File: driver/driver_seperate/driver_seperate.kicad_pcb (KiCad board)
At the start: 4 copper layers, 37.8 x 34.2 mm, 21 parts, among them IC1 MCT8316Z0TQRGFRQ1, J2 Motor, J3 Conn_01x05, J4 Conn_01x02

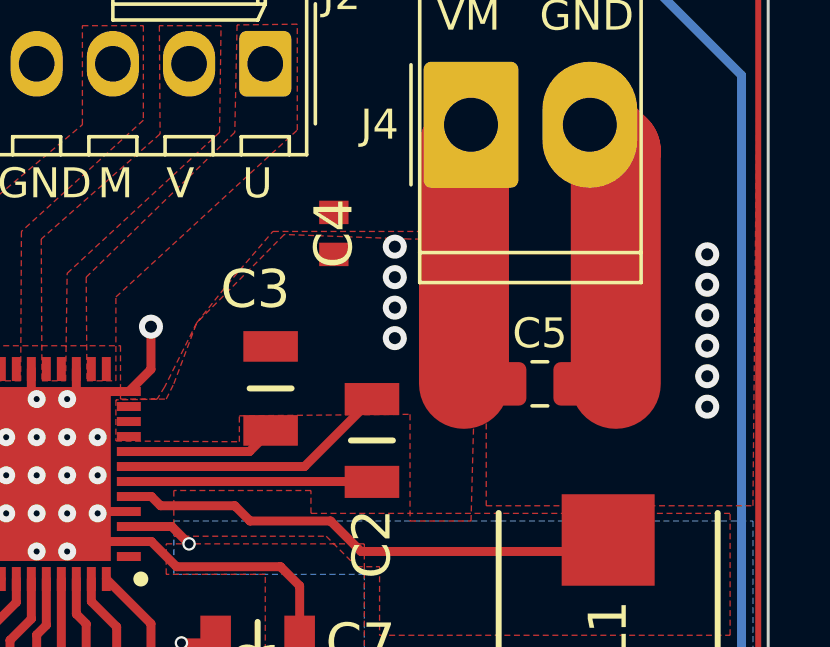
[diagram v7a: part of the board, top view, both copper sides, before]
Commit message: Move capacitor, change footprint to more common part
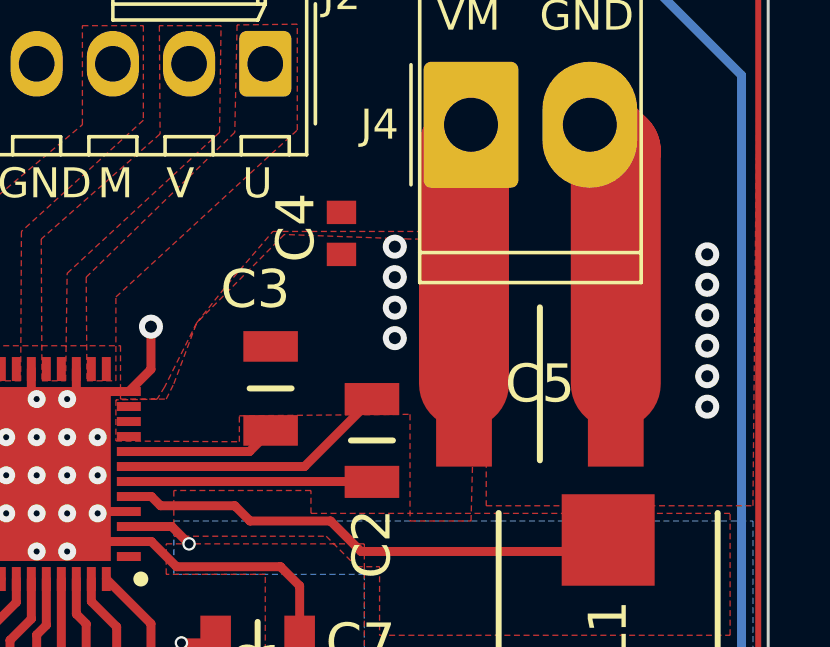
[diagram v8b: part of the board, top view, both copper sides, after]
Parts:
- C5: footprint Capacitor_SMD:C_0805_2012Metric -> SamacSys_Parts:CAPC6153X500N
- moved C4 0.25 mm to (132.6, 74.0)
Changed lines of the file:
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@@
   )
   (footprint "SamacSys_Parts:CAPC1608X95N" (layer "F.Cu")
-    (at 132.334 73.98 90)
+    (at 132.588 73.979 90)
     (descr "0603_2023-1")
     (tags "Capacitor")
@@
     (property "ki_keywords" "capacitor cap")
     (attr smd)
-    (fp_text reference "C4" (at 0 0 90) (layer "F.SilkS")
+    (fp_text reference "C4" (at 0.192 -1.524 90) (layer "F.SilkS")
         (effects (font (size 1.27 1.27) (thickness 0.254)))
     )
@@
     )
   )
-  (footprint "Capacitor_SMD:C_0805_2012Metric" (layer "F.Cu")
+  (footprint "SamacSys_Parts:CAPC6153X500N" (layer "F.Cu")
     (at 139.202 78.994)
-    (descr "Capacitor SMD 0805 (2012 Metric), square (rectangular) end terminal, IPC_7351 nominal, (Body size source: IPC-SM-782 page 76, https://www.pcb-3d.com/wordpress/wp-content/uploads/ipc-sm-782a_amendment_1_and_2.pdf, https://docs.google.com/spreadsheets/d/1BsfQQcO9C6DZCsRaXUlFlo91Tg2WpOkGARC1WS5S8t0/edit?usp=sharing), generated with kicad-footprint-generator")
-    (tags "capacitor")
+    (descr "KCM55 L=6.1mm W=5.3mm T=4.8mm")
+    (tags "Capacitor")
     (property "Sheetfile" "controller.kicad_sch")
     (property "Sheetname" "Motor Driver")
@@
     (property "ki_keywords" "cap capacitor")
     (attr smd)
-    (fp_text reference "C5" (at 0 -1.68) (layer "F.SilkS")
-        (effects (font (size 1 1) (thickness 0.15)))
-    )
-    (fp_text value "KCM55TR71H226MH01L" (at 0 1.68) (layer "F.Fab")
-        (effects (font (size 1 1) (thickness 0.15)))
+    (fp_text reference "C5" (at 0 0) (layer "F.SilkS")
+        (effects (font (size 1.27 1.27) (thickness 0.254)))
+    )
+    (fp_text value "KCM55TR71H226MH01L" (at 0 0) (layer "F.SilkS") hide
+        (effects (font (size 1.27 1.27) (thickness 0.254)))
     )
     (fp_text user "${REFERENCE}" (at 0 0) (layer "F.Fab")
-        (effects (font (size 0.5 0.5) (thickness 0.08)))
-    )
-    (fp_line (start -0.261252 -0.735) (end 0.261252 -0.735)
-      (stroke (width 0.12) (type solid)) (layer "F.SilkS"))
-    (fp_line (start -0.261252 0.735) (end 0.261252 0.735)
-      (stroke (width 0.12) (type solid)) (layer "F.SilkS"))
-    (fp_line (start -1.7 -0.98) (end 1.7 -0.98)
-      (stroke (width 0.05) (type solid)) (layer "F.CrtYd"))
-    (fp_line (start -1.7 0.98) (end -1.7 -0.98)
-      (stroke (width 0.05) (type solid)) (layer "F.CrtYd"))
-    (fp_line (start 1.7 -0.98) (end 1.7 0.98)
-      (stroke (width 0.05) (type solid)) (layer "F.CrtYd"))
-    (fp_line (start 1.7 0.98) (end -1.7 0.98)
-      (stroke (width 0.05) (type solid)) (layer "F.CrtYd"))
-    (fp_line (start -1 -0.625) (end 1 -0.625)
-      (stroke (width 0.1) (type solid)) (layer "F.Fab"))
-    (fp_line (start -1 0.625) (end -1 -0.625)
-      (stroke (width 0.1) (type solid)) (layer "F.Fab"))
-    (fp_line (start 1 -0.625) (end 1 0.625)
-      (stroke (width 0.1) (type solid)) (layer "F.Fab"))
-    (fp_line (start 1 0.625) (end -1 0.625)
-      (stroke (width 0.1) (type solid)) (layer "F.Fab"))
-    (pad "1" smd roundrect (at -0.95 0) (size 1 1.45) (layers "F.Cu" "F.Paste" "F.Mask") (roundrect_rratio 0.25)
+        (effects (font (size 1.27 1.27) (thickness 0.254)))
+    )
+    (fp_line (start 0 -2.55) (end 0 2.55)
+      (stroke (width 0.2) (type solid)) (layer "F.SilkS"))
+    (fp_line (start -3.61 -2.91) (end 3.61 -2.91)
+      (stroke (width 0.05) (type solid)) (layer "F.CrtYd"))
+    (fp_line (start -3.61 2.91) (end -3.61 -2.91)
+      (stroke (width 0.05) (type solid)) (layer "F.CrtYd"))
+    (fp_line (start 3.61 -2.91) (end 3.61 2.91)
+      (stroke (width 0.05) (type solid)) (layer "F.CrtYd"))
+    (fp_line (start 3.61 2.91) (end -3.61 2.91)
+      (stroke (width 0.05) (type solid)) (layer "F.CrtYd"))
+    (fp_line (start -3.05 -2.65) (end 3.05 -2.65)
+      (stroke (width 0.1) (type solid)) (layer "F.Fab"))
+    (fp_line (start -3.05 2.65) (end -3.05 -2.65)
+      (stroke (width 0.1) (type solid)) (layer "F.Fab"))
+    (fp_line (start 3.05 -2.65) (end 3.05 2.65)
+      (stroke (width 0.1) (type solid)) (layer "F.Fab"))
+    (fp_line (start 3.05 2.65) (end -3.05 2.65)
+      (stroke (width 0.1) (type solid)) (layer "F.Fab"))
+    (pad "1" smd rect (at -2.53 0) (size 1.86 5.52) (layers "F.Cu" "F.Paste" "F.Mask")
       (net 3 "/Motor Driver/VM") (pintype "passive"))
-    (pad "2" smd roundrect (at 0.95 0) (size 1 1.45) (layers "F.Cu" "F.Paste" "F.Mask") (roundrect_rratio 0.25)
+    (pad "2" smd rect (at 2.53 0) (size 1.86 5.52) (layers "F.Cu" "F.Paste" "F.Mask")
       (net 2 "GND") (pintype "passive"))
-    (model "${KICAD6_3DMODEL_DIR}/Capacitor_SMD.3dshapes/C_0805_2012Metric.wrl"
-      (offset (xyz 0 0 0))
-      (scale (xyz 1 1 1))
+    (model "KCM55TR71H226MH01L.stp"
+      (offset (xyz 0 0 0))
+      (scale (xyz 1 1 1))
